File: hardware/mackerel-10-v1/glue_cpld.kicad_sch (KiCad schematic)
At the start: 13 parts, among them J1 Conn_02x05_Odd_Even, X1 50MHz

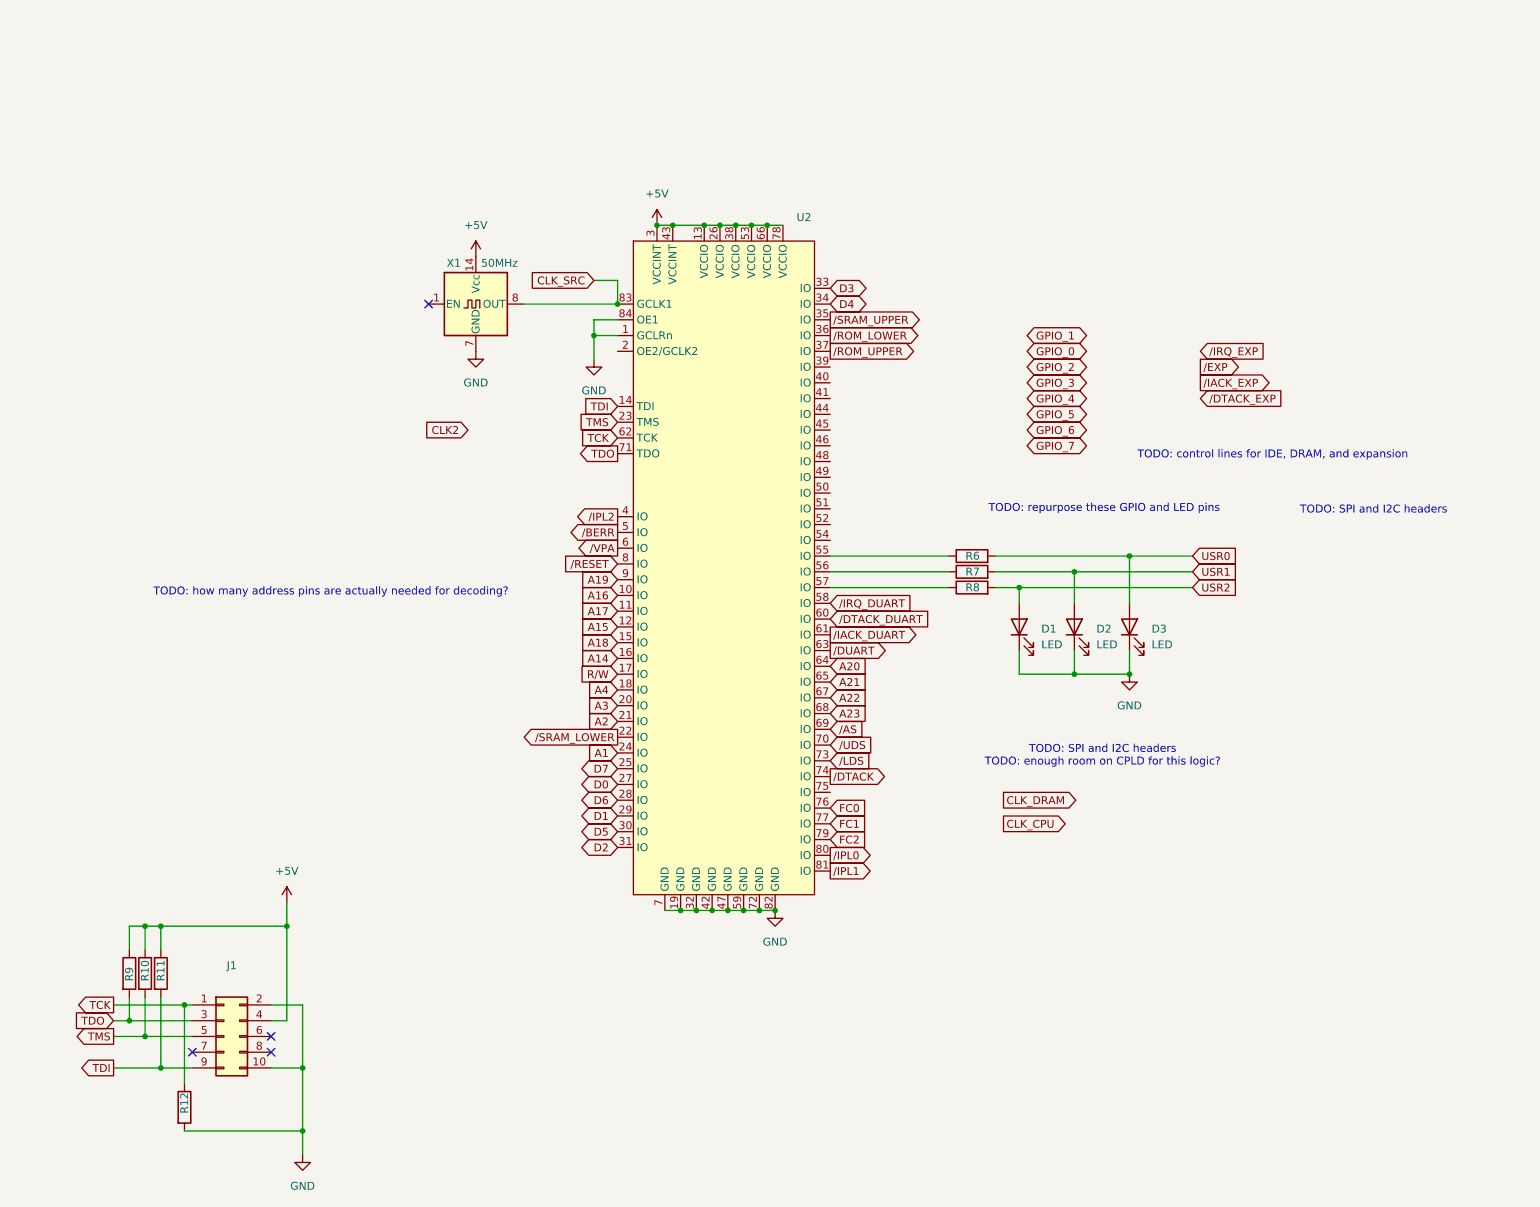
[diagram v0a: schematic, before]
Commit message: Rough layout of components on PCB
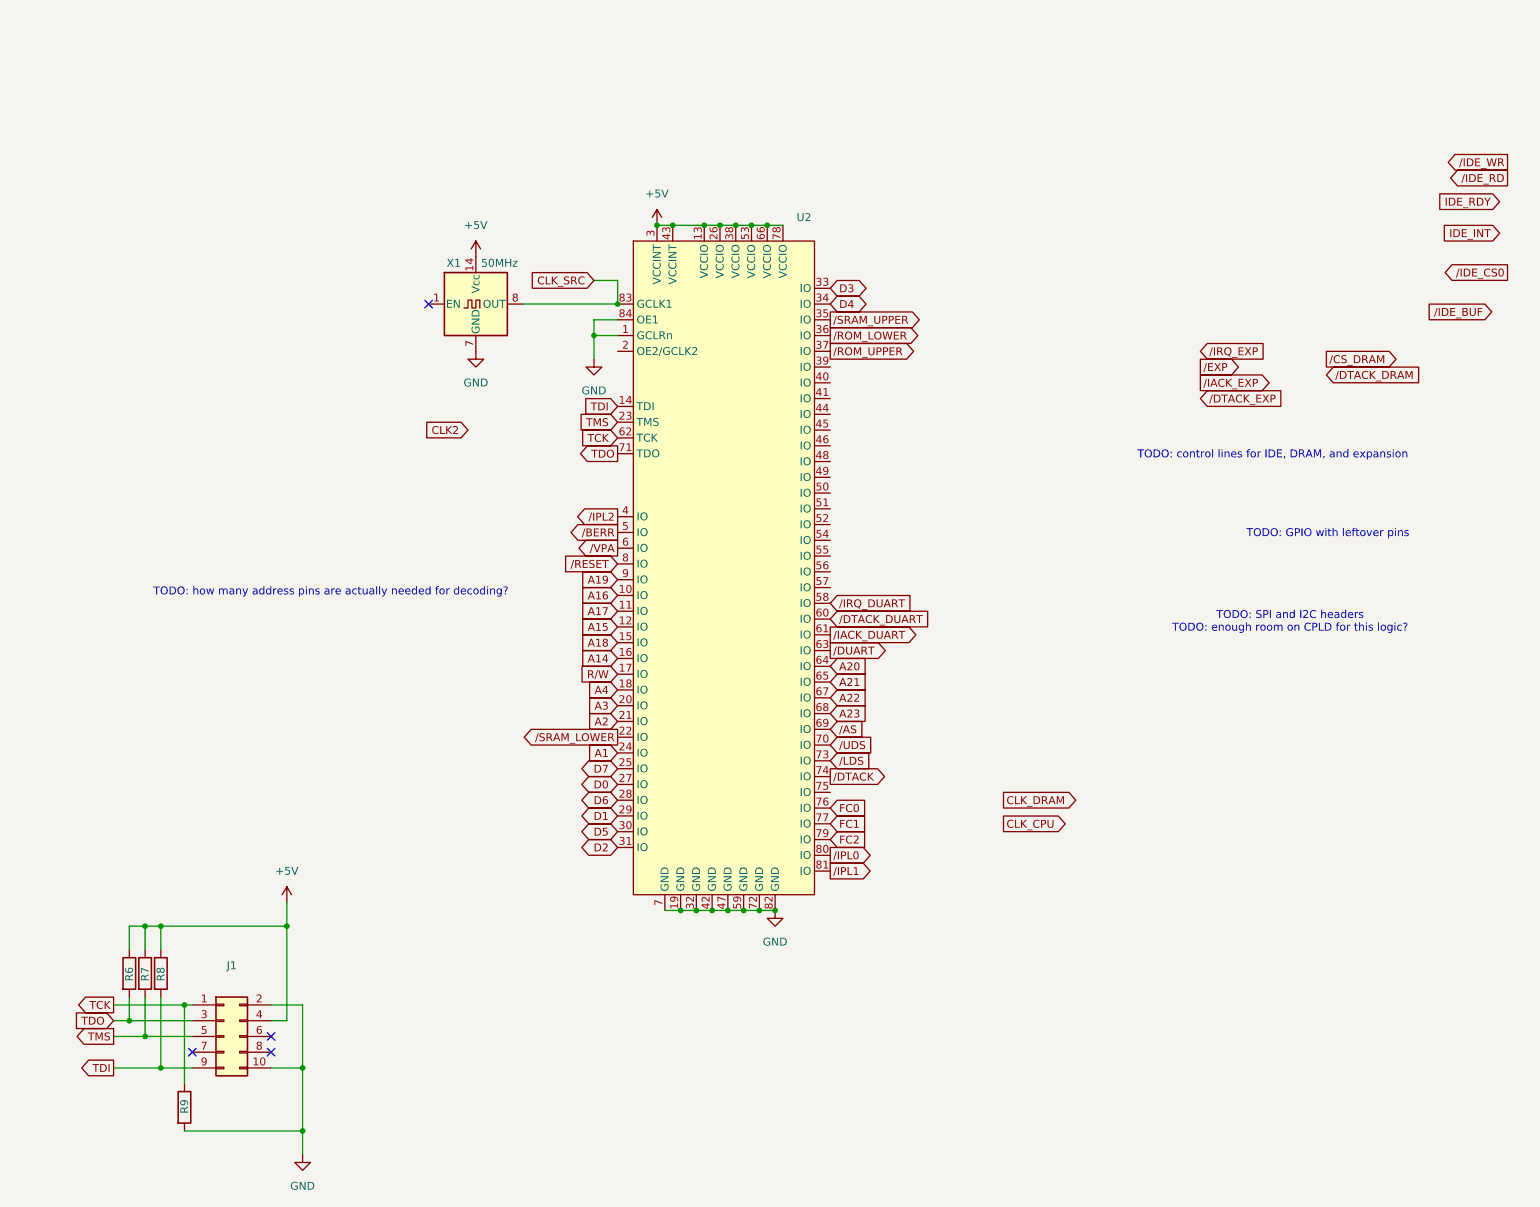
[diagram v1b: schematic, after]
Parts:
- removed D1, D2, D3: LED, LED_THT:LED_D5.0mm, symbol Device:LED
- removed R6, R7, R8: R, Resistor_THT:R_Axial_DIN0204_L3.6mm_D1.6mm_P5.08mm_Horizontal, symbol Device:R
- R6: renamed from R9; footprint Resistor_THT:R_Axial_DIN0204_L3.6mm_D1.6mm_P5.08mm_Horizontal -> Resistor_THT:R_Axial_DIN0207_L6.3mm_D2.5mm_P7.62mm_Horizontal
- R7: renamed from R10; footprint Resistor_THT:R_Axial_DIN0204_L3.6mm_D1.6mm_P5.08mm_Horizontal -> Resistor_THT:R_Axial_DIN0207_L6.3mm_D2.5mm_P7.62mm_Horizontal
- R8: renamed from R11; footprint Resistor_THT:R_Axial_DIN0204_L3.6mm_D1.6mm_P5.08mm_Horizontal -> Resistor_THT:R_Axial_DIN0207_L6.3mm_D2.5mm_P7.62mm_Horizontal
- R9: renamed from R12; footprint Resistor_THT:R_Axial_DIN0204_L3.6mm_D1.6mm_P5.08mm_Horizontal -> Resistor_THT:R_Axial_DIN0207_L6.3mm_D2.5mm_P7.62mm_Horizontal
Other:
- note added: "TODO: GPIO with leftover pins"
- note removed: "TODO: SPI and I2C headers"
- note removed: "TODO: repurpose these GPIO and LED pins"

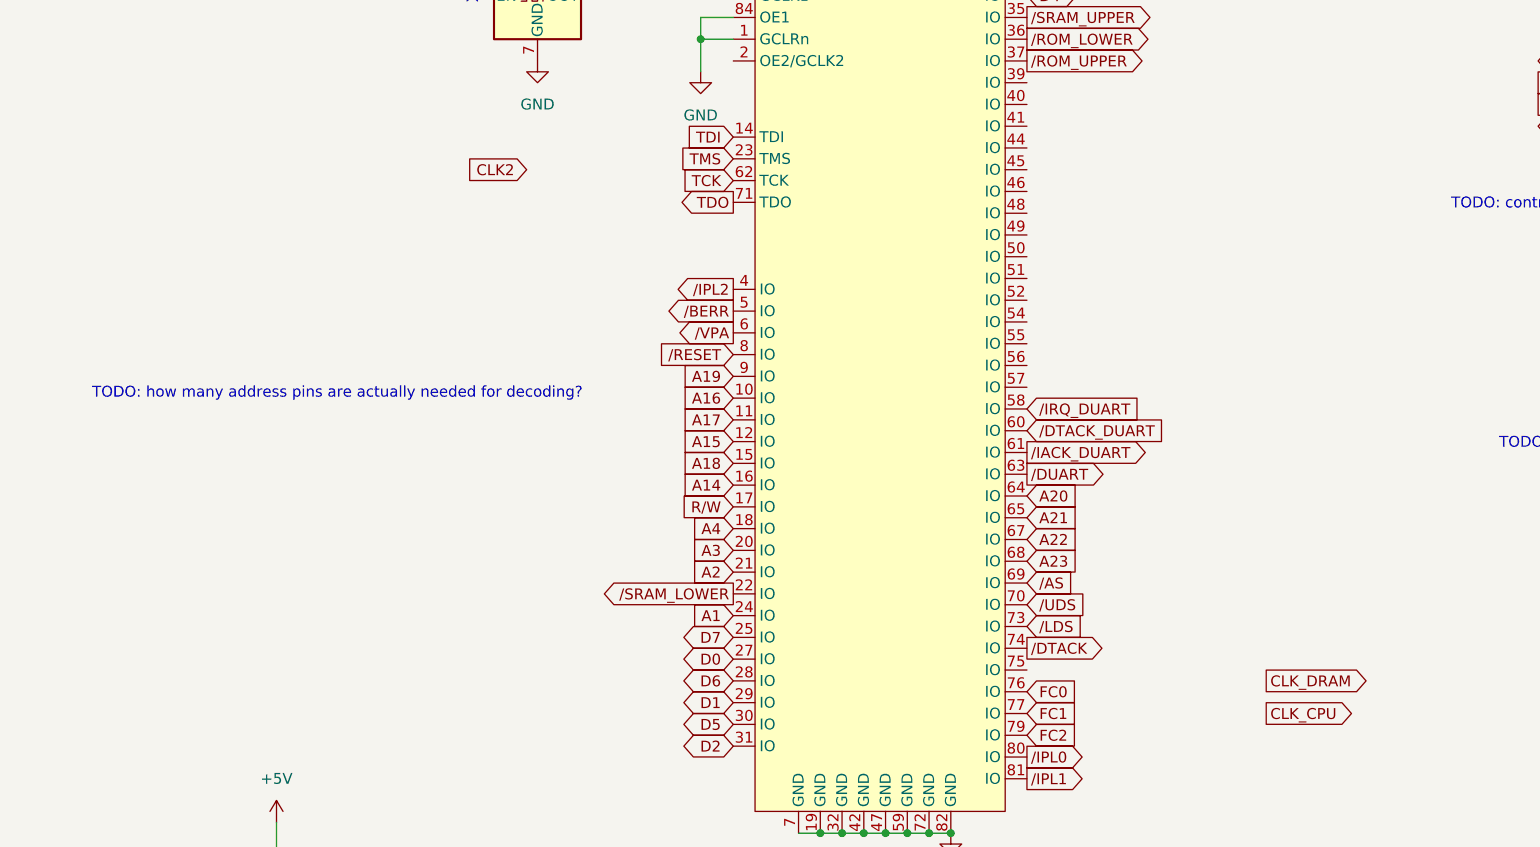
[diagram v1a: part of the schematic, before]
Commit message: Settled on mini ITX form factor
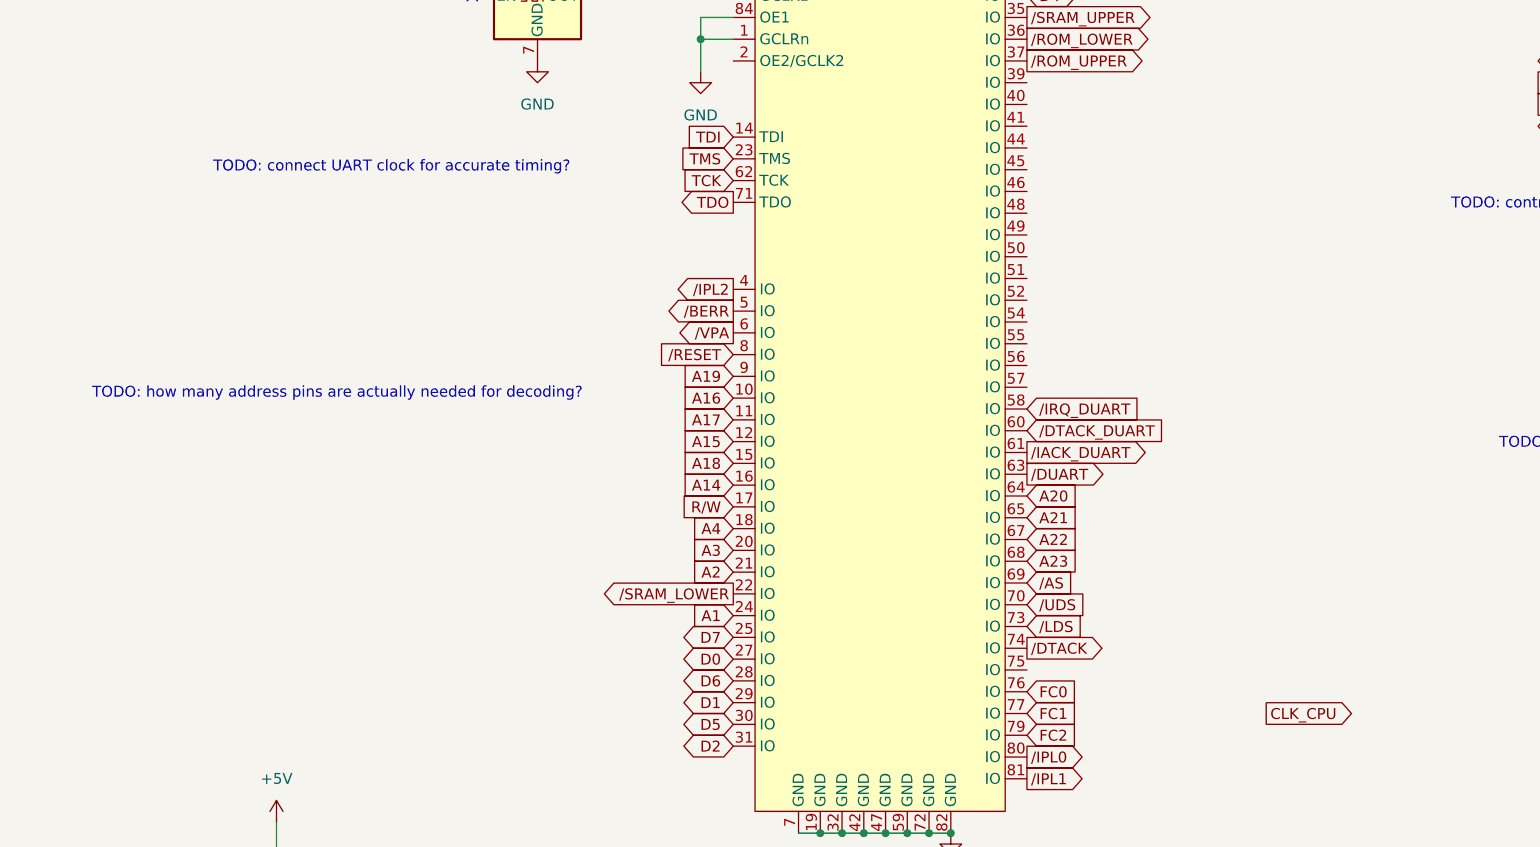
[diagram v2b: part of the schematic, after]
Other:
- note added: "TODO: connect UART clock for accurate timing?"
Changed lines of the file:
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@@
+		)
+	)
+	(text "TODO: connect UART clock for accurate timing?"
+		(exclude_from_sim no)
+		(at 73.152 70.866 0)
+		(effects
+			(font
+				(size 1.27 1.27)
+			)
 		)
 	)
@@
 		)
 	)
-	(global_label "CLK_DRAM"
-		(shape output)
-		(at 175.26 130.81 0)
-		(fields_autoplaced yes)
-		(effects
-			(font
-				(size 1.27 1.27)
-			)
-			(justify left)
-		)
-		(property "Intersheetrefs" "${INTERSHEET_REFS}"
-			(at 187.8609 130.81 0)
-			(effects
-				(font
-					(size 1.27 1.27)
-				)
-				(justify left)
-				(hide yes)
-			)
-		)
-	)
 	(global_label "A3"
 		(shape input)
@@
 				(hide yes)
 			)
-		)
-	)
-	(global_label "CLK2"
-		(shape input)
-		(at 88.9 71.12 180)
-		(fields_autoplaced yes)
-		(effects
-			(font
-				(size 1.27 1.27)
-			)
-			(justify right)
-		)
-		(property "Intersheetrefs" "${INTERSHEET_REFS}"
-			(at 81.1372 71.12 0)
-			(effects
-				(font
-					(size 1.27 1.27)
-				)
-				(justify right)
-				(hide yes)
-			)

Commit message: Another layout plan
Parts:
- added J12, J13, J15, J16: Conn_02x04_Odd_Even, Connector_IDC:IDC-Header_2x04_P2.54mm_Vertical, symbol Connector_Generic:Conn_02x04_Odd_Even
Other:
- note added: "SPI and I2C expansion"
- moved on the sheet: X1

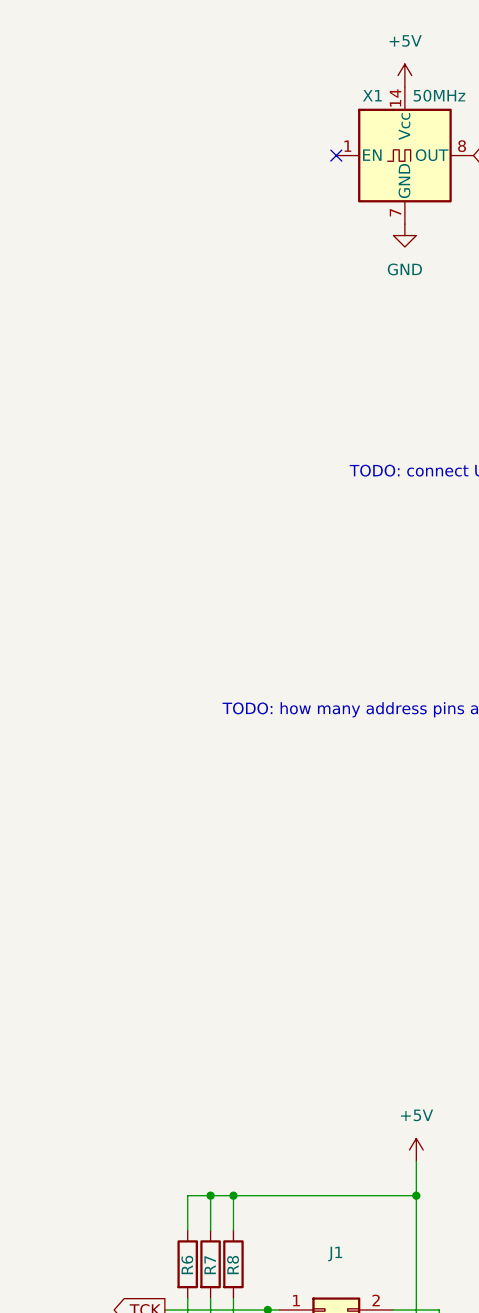
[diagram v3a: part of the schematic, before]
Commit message: half routed
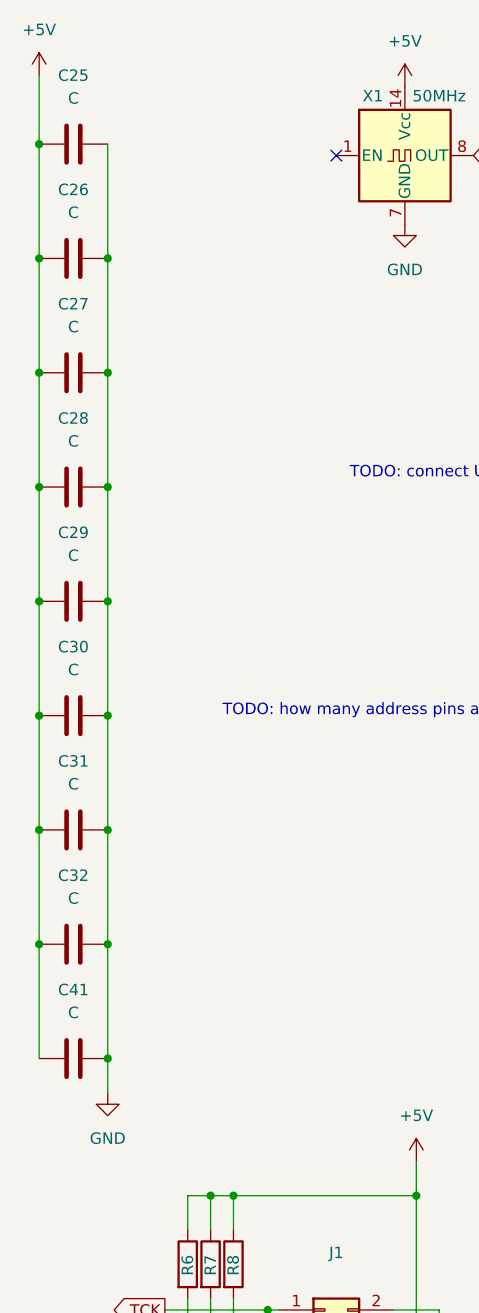
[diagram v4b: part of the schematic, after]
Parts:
- added C25, C26, C27, C28, C29, C30, C31, C32, C41: C, Capacitor_THT:C_Disc_D4.3mm_W1.9mm_P5.00mm, symbol Device:C
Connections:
- net +5V: now also C25.1, C26.1, C27.1, C28.1, C29.2, C30.2, C31.2, C32.2, C41.2
- net GND: now also C25.2, C26.2, C27.2, C28.2, C29.1, C30.1, C31.1, C32.1, C41.1
